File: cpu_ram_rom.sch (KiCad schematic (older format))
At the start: 9 parts, among them U3 AS6C4008A-55ZIN, U4 SST39SF040, U6 Z84C0010AEG

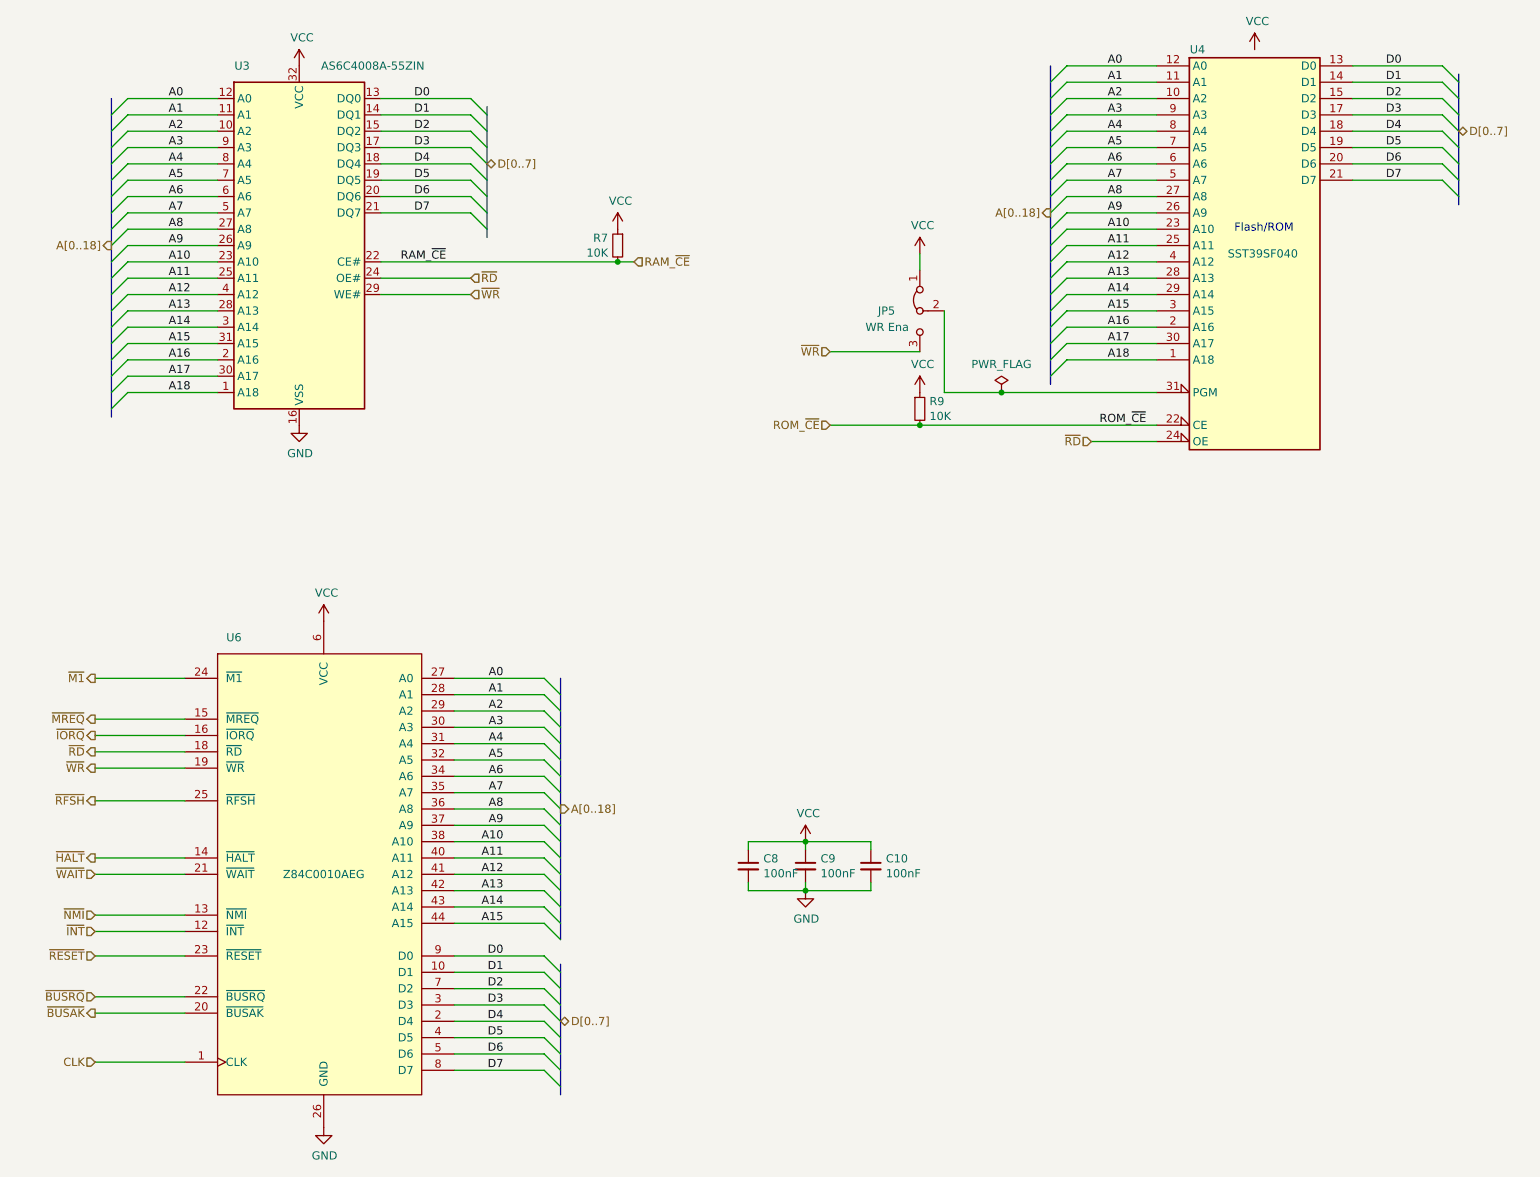
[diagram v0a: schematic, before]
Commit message: fixed clocks
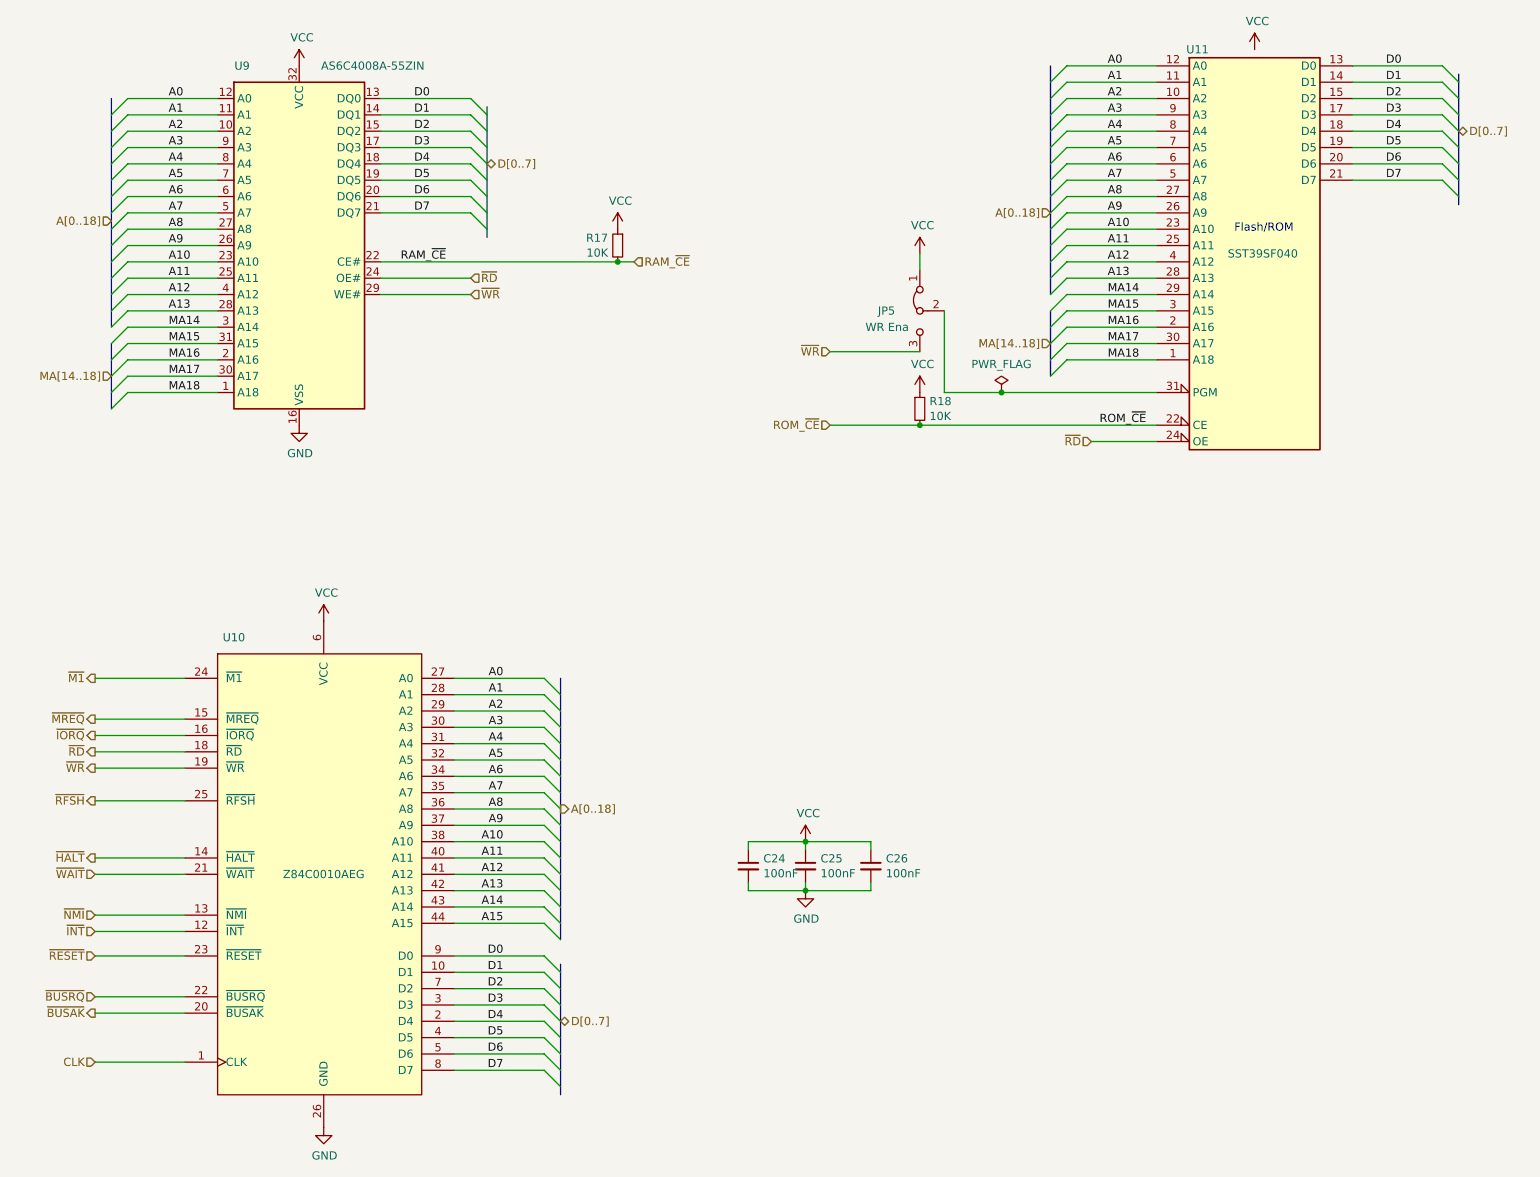
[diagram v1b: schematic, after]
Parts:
- renumbered C8 to C24, C9 to C25, C10 to C26, R7 to R17, R9 to R18, U6 to U10, U4 to U11, U3 to U9
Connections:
- net A14: no longer U11.29 (A14), U9.3 (A14)
- net A15: no longer U11.3 (A15), U9.31 (A15)
- net A16 renamed MA16
- net A17 renamed MA17
- net A18 renamed MA18
- new net MA14: U11.29 (A14), U9.3 (A14)
- new net MA15: U11.3 (A15), U9.31 (A15)
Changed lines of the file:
@@
 $Descr A4 11693 8268
 encoding utf-8
-Sheet 2 5
+Sheet 5 6
 Title ""
 Date ""
@@
 A13
 Text Label 2950 2400 0    50   ~ 0
-A14
+MA14
 Text Label 2950 2500 0    50   ~ 0
-A15
+MA15
 Entry Wire Line
 	2700 1000 2600 1100
@@
 Entry Wire Line
 	2700 2500 2600 2600
-Text HLabel 2600 1900 0    50   Output ~ 0
+Text HLabel 2600 1750 0    50   Input ~ 0
 A[0..18]
 Entry Wire Line
@@
 	3250 2800 2700 2800
 Text Label 2950 2700 0    50   ~ 0
-A17
+MA17
 Text Label 2950 2800 0    50   ~ 0
-A18
+MA18
 Entry Wire Line
 	2700 2600 2600 2700
@@
 	3250 2600 2700 2600
 Text Label 2950 2600 0    50   ~ 0
-A16
+MA16
 Wire Wire Line
 	4250 2200 4800 2200
@@
 AR Path="/5CFABACD/5D90DF01" Ref="#PWR?"  Part="1"
 AR Path="/5CF9C1ED/5D90DF01" Ref="#PWR?"  Part="1"
-AR Path="/5D6224DC/5D90DF01" Ref="#PWR020"  Part="1"
-F 0 "#PWR020" H 3750 2750 50  0001 C CNN
+AR Path="/5D6224DC/5D90DF01" Ref="#PWR074"  Part="1"
+F 0 "#PWR074" H 3750 2750 50  0001 C CNN
 F 1 "GND" H 3755 2827 50  0000 C CNN
 F 2 "" H 3750 3000 50  0001 C CNN
@@
 $EndComp
 $Comp
-L THS-80:Z84C0010AEG U6
+L THS-80:Z84C0010AEG U10
 U 1 1 5F309FF5
 P 3900 5750
-F 0 "U6" H 3350 7200 50  0000 C CNN
+F 0 "U10" H 3350 7200 50  0000 C CNN
 F 1 "Z84C0010AEG" H 3900 5750 50  0000 C CNN
 F 2 "Package_QFP:LQFP-44_10x10mm_P0.8mm" H 950 6750 50  0001 L CNN
@@
 AR Path="/5CFABACD/5F33A976" Ref="#PWR?"  Part="1"
 AR Path="/5CF9C1ED/5F33A976" Ref="#PWR?"  Part="1"
-AR Path="/5D6224DC/5F33A976" Ref="#PWR027"  Part="1"
-F 0 "#PWR027" H 3900 7050 50  0001 C CNN
+AR Path="/5D6224DC/5F33A976" Ref="#PWR076"  Part="1"
+F 0 "#PWR076" H 3900 7050 50  0001 C CNN
 F 1 "GND" H 3905 7127 50  0000 C CNN
 F 2 "" H 3900 7300 50  0001 C CNN
@@
 P 6850 5850
 AR Path="/5D70CA34/5FC53564" Ref="#PWR?"  Part="1"
-AR Path="/5D6224DC/5FC53564" Ref="#PWR024"  Part="1"
-F 0 "#PWR024" H 6850 5600 50  0001 C CNN
+AR Path="/5D6224DC/5FC53564" Ref="#PWR079"  Part="1"
+F 0 "#PWR079" H 6850 5600 50  0001 C CNN
 F 1 "GND" H 6855 5677 50  0000 C CNN
 F 2 "" H 6850 5850 50  0001 C CNN
@@
 $EndComp
 $Comp
-L Device:R_Small R9
+L Device:R_Small R18
 U 1 1 5D959555
 P 7550 2900
-F 0 "R9" H 7609 2946 50  0000 L CNN
+F 0 "R18" H 7609 2946 50  0000 L CNN
 F 1 "10K" H 7609 2855 50  0000 L CNN
 F 2 "Resistor_SMD:R_0603_1608Metric_Pad1.05x0.95mm_HandSolder" H 7550 2900 50  0001 C CNN
@@
 $EndComp
 $Comp
-L Device:R_Small R7
+L Device:R_Small R17
 U 1 1 5D966170
 P 5700 1900
-F 0 "R7" H 5759 1946 50  0000 L CNN
+F 0 "R17" H 5759 1946 50  0000 L CNN
 F 1 "10K" H 5759 1855 50  0000 L CNN
 F 2 "Resistor_SMD:R_0603_1608Metric_Pad1.05x0.95mm_HandSolder" H 5700 1900 50  0001 C CNN
@@
 Text HLabel 8600 3100 0    50   Input ~ 0
 ~RD
-Wire Wire Line
-	8450 2500 9000 2500
-Text Label 8700 2400 0    50   ~ 0
-A16
-Wire Wire Line
-	9000 2400 8450 2400
-Entry Wire Line
-	8450 2600 8350 2700
-Entry Wire Line
-	8450 2500 8350 2600
-Entry Wire Line
-	8450 2400 8350 2500
-Text Label 8700 2600 0    50   ~ 0
-A18
-Text Label 8700 2500 0    50   ~ 0
-A17
-Wire Wire Line
-	9000 2600 8450 2600
-Text HLabel 8350 1700 0    50   Output ~ 0
+Text HLabel 8350 1700 0    50   Input ~ 0
 A[0..18]
 Entry Wire Line
-	8450 2300 8350 2400
-Entry Wire Line
-	8450 2200 8350 2300
-Entry Wire Line
 	8450 2100 8350 2200
 Entry Wire Line
@@
 Entry Wire Line
 	8450 800  8350 900
-Text Label 8700 2300 0    50   ~ 0
-A15
-Text Label 8700 2200 0    50   ~ 0
-A14
 Text Label 8700 2100 0    50   ~ 0
 A13
@@
 A0
 Wire Wire Line
-	9000 2300 8450 2300
-Wire Wire Line
-	9000 2200 8450 2200
-Wire Wire Line
 	9000 2100 8450 2100
 Wire Wire Line
@@
 Flash/ROM
 $Comp
-L Memory_Flash:SST39SF040 U4
+L Memory_Flash:SST39SF040 U11
 U 1 1 5D653323
 P 9600 2000
-F 0 "U4" H 9250 3300 50  0000 C CNN
+F 0 "U11" H 9250 3300 50  0000 C CNN
 F 1 "SST39SF040" H 9650 2050 50  0000 C CNN
 F 2 "Package_LCC:PLCC-32_11.4x14.0mm_P1.27mm" H 9600 2300 50  0001 C CNN
@@
 Connection ~ 7550 3000
 $Comp
-L Device:C_Small C8
+L Device:C_Small C24
 U 1 1 5F181CA3
 P 6500 5700
-F 0 "C8" H 6592 5746 50  0000 L CNN
+F 0 "C24" H 6592 5746 50  0000 L CNN
 F 1 "100nF" H 6592 5655 50  0000 L CNN
 F 2 "Capacitor_SMD:C_0603_1608Metric_Pad1.05x0.95mm_HandSolder" H 6500 5700 50  0001 C CNN
@@
 $EndComp
 $Comp
-L Device:C_Small C9
+L Device:C_Small C25
 U 1 1 5F182ACB
 P 6850 5700
-F 0 "C9" H 6942 5746 50  0000 L CNN
+F 0 "C25" H 6942 5746 50  0000 L CNN
 F 1 "100nF" H 6942 5655 50  0000 L CNN
 F 2 "Capacitor_SMD:C_0603_1608Metric_Pad1.05x0.95mm_HandSolder" H 6850 5700 50  0001 C CNN
@@
 $EndComp
 $Comp
-L Device:C_Small C10
+L Device:C_Small C26
 U 1 1 5F189729
 P 7250 5700
-F 0 "C10" H 7342 5746 50  0000 L CNN
+F 0 "C26" H 7342 5746 50  0000 L CNN
 F 1 "100nF" H 7342 5655 50  0000 L CNN
 F 2 "Capacitor_SMD:C_0603_1608Metric_Pad1.05x0.95mm_HandSolder" H 7250 5700 50  0001 C CNN
@@
 P 7550 2800
 AR Path="/5DC9BD0A" Ref="#PWR?"  Part="1"
-AR Path="/5D6224DC/5DC9BD0A" Ref="#PWR0106"  Part="1"
-F 0 "#PWR0106" H 7550 2650 50  0001 C CNN
+AR Path="/5D6224DC/5DC9BD0A" Ref="#PWR081"  Part="1"
+F 0 "#PWR081" H 7550 2650 50  0001 C CNN
 F 1 "VCC" H 7567 2973 50  0000 C CNN
 F 2 "" H 7550 2800 50  0001 C CNN
@@
 P 7550 1950
 AR Path="/5DCA243D" Ref="#PWR?"  Part="1"
-AR Path="/5D6224DC/5DCA243D" Ref="#PWR0107"  Part="1"
-F 0 "#PWR0107" H 7550 1800 50  0001 C CNN
+AR Path="/5D6224DC/5DCA243D" Ref="#PWR080"  Part="1"
+F 0 "#PWR080" H 7550 1800 50  0001 C CNN
 F 1 "VCC" H 7567 2123 50  0000 C CNN
 F 2 "" H 7550 1950 50  0001 C CNN
@@
 P 3750 800
 AR Path="/5DCD0880" Ref="#PWR?"  Part="1"
-AR Path="/5D6224DC/5DCD0880" Ref="#PWR0108"  Part="1"
-F 0 "#PWR0108" H 3750 650 50  0001 C CNN
+AR Path="/5D6224DC/5DCD0880" Ref="#PWR073"  Part="1"
+F 0 "#PWR073" H 3750 650 50  0001 C CNN
 F 1 "VCC" H 3767 973 50  0000 C CNN
 F 2 "" H 3750 800 50  0001 C CNN
@@
 P 5700 1800
 AR Path="/5DCDDE0E" Ref="#PWR?"  Part="1"
-AR Path="/5D6224DC/5DCDDE0E" Ref="#PWR0109"  Part="1"
-F 0 "#PWR0109" H 5700 1650 50  0001 C CNN
+AR Path="/5D6224DC/5DCDDE0E" Ref="#PWR077"  Part="1"
+F 0 "#PWR077" H 5700 1650 50  0001 C CNN
 F 1 "VCC" H 5717 1973 50  0000 C CNN
 F 2 "" H 5700 1800 50  0001 C CNN
@@
 P 3900 4200
 AR Path="/5DCEC440" Ref="#PWR?"  Part="1"
-AR Path="/5D6224DC/5DCEC440" Ref="#PWR0110"  Part="1"
-F 0 "#PWR0110" H 3900 4050 50  0001 C CNN
+AR Path="/5D6224DC/5DCEC440" Ref="#PWR075"  Part="1"
+F 0 "#PWR075" H 3900 4050 50  0001 C CNN
 F 1 "VCC" H 3917 4373 50  0000 C CNN
 F 2 "" H 3900 4200 50  0001 C CNN
@@
 P 9600 700
 AR Path="/5DCF306D" Ref="#PWR?"  Part="1"
-AR Path="/5D6224DC/5DCF306D" Ref="#PWR0111"  Part="1"
-F 0 "#PWR0111" H 9600 550 50  0001 C CNN
+AR Path="/5D6224DC/5DCF306D" Ref="#PWR082"  Part="1"
+F 0 "#PWR082" H 9600 550 50  0001 C CNN
 F 1 "VCC" H 9617 873 50  0000 C CNN
 F 2 "" H 9600 700 50  0001 C CNN
@@
 P 6850 5550
 AR Path="/5DD0030A" Ref="#PWR?"  Part="1"
-AR Path="/5D6224DC/5DD0030A" Ref="#PWR0112"  Part="1"
-F 0 "#PWR0112" H 6850 5400 50  0001 C CNN
+AR Path="/5D6224DC/5DD0030A" Ref="#PWR078"  Part="1"
+F 0 "#PWR078" H 6850 5400 50  0001 C CNN
 F 1 "VCC" H 6867 5723 50  0000 C CNN
 F 2 "" H 6850 5550 50  0001 C CNN
@@
 $EndComp
 $Comp
-L THS-80-rescue:AS6C4008A-55ZIN-Memory_RAM U3
+L THS-80-rescue:AS6C4008A-55ZIN-Memory_RAM U9
 U 1 1 5DA31E6C
 P 3750 1900
-F 0 "U3" H 3400 3000 50  0000 C CNN
+F 0 "U9" H 3400 3000 50  0000 C CNN
 F 1 "AS6C4008A-55ZIN" H 4200 3000 50  0000 C CNN
 F 2 "Package_SO:TSOP-II-32_21.0x10.2mm_P1.27mm" H 3750 2000 50  0001 C CNN
@@
 	7000 3000 7550 3000
 $Comp
-L power:PWR_FLAG #FLG02
+L power:PWR_FLAG #FLG01
 U 1 1 5E91C5ED
 P 8050 2800
-F 0 "#FLG02" H 8050 2875 50  0001 C CNN
+F 0 "#FLG01" H 8050 2875 50  0001 C CNN
 F 1 "PWR_FLAG" H 8050 2973 50  0000 C CNN
 F 2 "" H 8050 2800 50  0001 C CNN
@@
 Wire Wire Line
 	8050 2800 7700 2800
+Text HLabel 2600 2700 0    50   Input ~ 0
+MA[14..18]
+Wire Wire Line
+	9000 2300 8450 2300
+Text Label 8700 2300 0    50   ~ 0
+MA15
+Entry Wire Line
+	8450 2200 8350 2300
+Entry Wire Line
+	8450 2300 8350 2400
+Wire Wire Line
+	9000 2500 8450 2500
+Wire Wire Line
+	9000 2600 8450 2600
+Text Label 8700 2500 0    50   ~ 0
+MA17
+Text Label 8700 2600 0    50   ~ 0
+MA18
+Entry Wire Line
+	8450 2400 8350 2500
+Entry Wire Line
+	8450 2500 8350 2600
+Entry Wire Line
+	8450 2600 8350 2700
+Wire Wire Line
+	9000 2400 8450 2400
+Text Label 8700 2400 0    50   ~ 0
+MA16
+Text HLabel 8350 2500 0    50   Input ~ 0
+MA[14..18]
+Wire Wire Line
+	9000 2200 8450 2200
+Text Label 8700 2200 0    50   ~ 0
+MA14
+Wire Bus Line
+	2600 2500 2600 2900
+Wire Bus Line
+	8350 2300 8350 2700
 Wire Bus Line
 	10850 850  10850 1650
@@
 	5350 6300 5350 7100
 Wire Bus Line
-	2600 1000 2600 2950
+	2600 1000 2600 2400
+Wire Bus Line
+	8350 800  8350 2200
 Wire Bus Line
 	5350 4550 5350 6150
-Wire Bus Line
-	8350 800  8350 2750
 $EndSCHEMATC
